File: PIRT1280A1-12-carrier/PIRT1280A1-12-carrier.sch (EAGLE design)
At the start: 124 parts, among them J1 5-1734592-0, U1 LT3042IMSE#TRPBF, U2 LT3042IMSE#TRPBF, U3 LT3042IMSE#TRPBF, U4 LT3042IMSE#TRPBF, U5 LT3042IMSE#TRPBF, U6 DS90CR218AMTD/NOPBMTD48_TEX-L

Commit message: mostly finished with PIRT1280 carrier
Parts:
- removed C38: 10u, oresat-rcl:C-EU0603-C-NOSILK
- removed SJ11, SJ12, SJ13, SJ14, SJ15, SJ22: SOLDERJUMPERNC, SparkFun-Passives:SOLDERJUMPERNC
- removed TEC+, TEC-, VDETCOM, VPH, VPL, VPOS, VPOUT: TEST-POINT_SMD-SMD-10SN, oresat-misc:TEST-POINT_SMD-SMD-10SN
- removed TP39, TP40, TP41, TP42, TP43: TEST-POINT-LARGE-SQUARE, oresat-misc:TEST-POINT-LARGE-SQUARE
- added C16: 1u, oresat-rcl:C-EU0603-A
- added C17: 0.1u, oresat-rcl:C-EU0603-A
- added C18: 1n, oresat-rcl:C-EU0402-C-NOSILK
- added D1: GREEN, SparkFun-LED:LED-GREEN0603
- added J10, J3, J4, J5, J6: 455-1750-1-ND, SparkFun-Connectors:CONN_03
- added J11: USB_A_SMT_FEMALE, SparkFun-Connectors:USB_A_SMT_FEMALE
- added J12: (no value), SparkFun-Connectors:CONN_025MM
- added J13: POWER_JACK, SparkFun-Connectors:POWER_JACK
- added J2: (no value), SparkFun-Connectors:CONN_02
- added J7: (no value), SparkFun-Connectors:CONN_05
- added J8: (no value), SparkFun-Connectors:CONN_13
- added J9: 5-1734592-0, J-TEConnectivity-X-1734592-X:5-1734592-0
- added JP1, JP100, JP101: JUMPER-SMT_2_NC_TRACE_NO-SILK, SparkFun-Jumpers:JUMPER-SMT_2_NC_TRACE_NO-SILK
- added Q1: 35A/25V/8.5mΩ, Q-Fairchild-FDD8780-MOSFET-NCH:MOSFET-NCH-FDD8780
- added R100, R101, R21, R22, R23, R24, R25, R26: 100, oresat-rcl:R-US_0402-C-NOSILK
- added R12: NP, oresat-rcl:R-US_0603-A
- added R19: 10k, R-Panasonic-EXB_A10PXXXJ:EXB-A10P391JC_ARRAY_EXBA-M
- added R20: TBD, oresat-rcl:R-US_0603-A
- added REFCLK, THERM+, THERM-, TP9: TEST-POINT-LARGE-SQUARE, oresat-misc:TEST-POINT-LARGE-SQUARE
- added TP100, TP101, TP102, TP103, TP104, TP105, TP106, TP107: TEST-POINT-SMD-0.5MM, oresat-misc:TEST-POINT-SMD-0.5MM
- added U7: DS90CR218AMTD/NOPBMTD48_TEX-L, U-TI-DS90CR218-LVDSReceiver:DS90CR218AMTD/NOPBMTD48_TEX-L
- added X1: 16MHz, X-OSCILLATOR-GENERIC:OSC_GENERIC_2.5X2.0
- C1, C10, C2, C3, C4, C5, C6, C7, C8, C9: device oresat-rcl:C-EU0402-A-NOSILK -> oresat-rcl:C-EU0603-A
- C11, C12, C13, C14, C15: value 4.7u -> 0.47u; device oresat-rcl:C-EU0402-A-NOSILK -> oresat-rcl:C-EU0603-A
- C19, C22: value 1n -> 10n; DPN 490-6350-1-ND -> 399-7842-1-ND; MFR Murata -> Kemet; MPN GRM155R71H102KA01J -> C0603C103M5RACTU
- C20, C23: value 1n -> 100n; DPN 490-6350-1-ND -> 399-1177-1-ND; MFR Murata -> Kemet; MPN GRM155R71H102KA01J -> C0805C104Z5VACTU
- C24: value 1n -> 10u; device oresat-rcl:C-EU0402-C-NOSILK -> oresat-rcl:C-EU0603-C-NOSILK; DPN 490-6350-1-ND -> 490-14372-1-ND; MPN GRM155R71H102KA01J -> GRM188R61A106KE69J
- C25, C30: value 10n -> 100n; DPN 399-7842-1-ND -> 399-1177-1-ND; MPN C0603C103M5RACTU -> C0805C104Z5VACTU
- C27, C28: value 10n -> 1n; DPN 399-7842-1-ND -> 490-6350-1-ND; MFR Kemet -> Murata; MPN C0603C103M5RACTU -> GRM155R71H102KA01J
- C31, C36: value 100n -> 1n; DPN 399-1177-1-ND -> 490-6350-1-ND; MFR Kemet -> Murata; MPN C0805C104Z5VACTU -> GRM155R71H102KA01J
- C32, C35: value 100n -> 10n; DPN 399-1177-1-ND -> 399-7842-1-ND; MPN C0805C104Z5VACTU -> C0603C103M5RACTU
- J1: value 5-1734592-0 -> 455-1750-1-ND; device J-TEConnectivity-X-1734592-X:5-1734592-0 -> SparkFun-Connectors:CONN_03
- R1: value (none) -> 1k; device oresat-rcl:R-US_0603-A-NOSILK -> oresat-rcl:R-US_0603-A
- R10, R11, R8, R9: value 100 -> NP; device oresat-rcl:R-US_0402-C-NOSILK -> oresat-rcl:R-US_0603-A; DIS Dgi-Key -> (none); DPN 311-100MCT-ND -> (none); MFR Yageo -> (none); MPN RC0201FR-07100RL -> (none)
- R13, R14: value 100 -> 0; device oresat-rcl:R-US_0402-C-NOSILK -> oresat-rcl:R-US_0603-A; DIS Dgi-Key -> (none); DPN 311-100MCT-ND -> (none); MFR Yageo -> (none); MPN RC0201FR-07100RL -> (none)
- R15, R17: device oresat-rcl:R-US_0603-A-NOSILK -> oresat-rcl:R-US_0603-A
- R16: value (none) -> 0; device oresat-rcl:R-US_0603-A-NOSILK -> oresat-rcl:R-US_0603-A
- R18: value 100 -> 20k; device oresat-rcl:R-US_0402-C-NOSILK -> oresat-rcl:R-US_0805-A; DIS Dgi-Key -> (none); DPN 311-100MCT-ND -> (none); MFR Yageo -> (none); MPN RC0201FR-07100RL -> (none)
- R2: value 0 -> 10k; device oresat-rcl:R-US_0603-A-NOSILK -> R-Panasonic-EXB-2HV103JV:EXB-2HV103JV
- R3: value (none) -> 29.4k; device oresat-rcl:R-US_0603-A-NOSILK -> oresat-rcl:R-US_0603-A
- R4: value (none) -> 9.09k; device oresat-rcl:R-US_0603-A-NOSILK -> oresat-rcl:R-US_0603-A
- R5: value 0 -> 16.2k; device oresat-rcl:R-US_0603-A-NOSILK -> oresat-rcl:R-US_0603-A
- R6: value (none) -> 33.2k; device oresat-rcl:R-US_0603-A-NOSILK -> oresat-rcl:R-US_0603-A
- R7: value 0 -> 33.2k; device oresat-rcl:R-US_0603-A-NOSILK -> oresat-rcl:R-US_0603-A
- SJ1, SJ10, SJ2, SJ3, SJ4, SJ5, SJ6, SJ7, SJ8, SJ9: value SOLDERJUMPERNC -> JUMPER-SMT_2_NC_TRACE_NO-SILK; device SparkFun-Passives:SOLDERJUMPERNC -> SparkFun-Jumpers:JUMPER-SMT_2_NC_TRACE_NO-SILK
- U6: value DS90CR218AMTD/NOPBMTD48_TEX-L -> LM2901QPWRQ1PW14-M; device U-TI-DS90CR218-LVDSReceiver:DS90CR218AMTD/NOPBMTD48_TEX-L -> U-TI-LM2901:LM2901QPWRQ1PW14-M
- renumbered U$1 to U$2
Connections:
- removed net CLK: U$2G$1.P1_20, U6.RXCLKOUT
- removed net D0: U$2G$1.P1_36, U6.RXOUT0
- removed net D1: U$2G$1.P1_33, U6.RXOUT1
- removed net D2: U$2G$2.P2_32, U6.RXOUT2
- removed net D3: U$2G$2.P2_30, U6.RXOUT3
- removed net D4: U$2G$1.P1_31, U6.RXOUT4
- removed net D5: U$2G$2.P2_34, U6.RXOUT5
- removed net D6: U$2G$2.P2_28, U6.RXOUT6
- removed net D7: U$2G$1.P1_29, U6.RXOUT7
- removed net N$30: SJ11.1, TP32.1, U4.EN/UV
- removed net N$34: U6.!PWR_DWN
- removed net SDCLK: J1.49, TP4.1
- removed net SDIN: J1.50, TP5.1
- removed net SDOUT: J1.48, TP6.1
- removed net USB_D+: U$2G$1.P1_11
- removed net USB_D-: U$2G$1.P1_9
- new net !PWR_DWN: J3.2, R19.11, U7.!PWR_DWN
- new net 1.8V-A: R20.2, U$2G$1.P1_18
- new net N$1: R2.1, R2.2
- new net N$2: R2.15, R2.3, U6.4IN-
- new net N$270: D1.A, R1.1
- new net N$3: R2.14, R2.4, U6.3IN-
- new net N$4: R2.13, R2.5, U6.2IN-
- new net N$41: J13.PWR, U$2G$1.P1_1
- new net N$44: R2.11, R2.12, U6.1IN-
- new net N$47: TP100.TP, U7.RXOUT7
- new net N$48: TP101.TP, U7.RXOUT8
- new net N$49: TP102.TP, U7.RXOUT9
- new net N$5: C16.1, R18.2, U6.1IN+, U6.2IN+, U6.3IN+, U6.4IN+
- new net N$50: TP103.TP, U7.RXOUT10
- new net N$51: TP104.TP, U7.RXOUT11
- new net N$52: TP105.TP, U7.RXOUT12
- new net N$53: TP106.TP, U7.RXOUT13
- new net N$54: TP107.TP, U7.RXOUT14
- new net N$55: J2.2, U$2G$1.P1_34
- new net N$56: J10.1, Q1.D
- new net N$58: J3.1, U$2G$2.P2_20
- new net N$6: R2.6, R2.7
- new net N$8: JP100.1, U$2G$1.P1_5
- new net PRU0: J8.2, U$2G$1.P1_36, U7.RXOUT0
- new net PRU1: J8.3, U$2G$1.P1_33, U7.RXOUT1
- new net PRU14_OUT: J8.11, U$2G$2.P2_24
- new net PRU15_OUT: J8.12, U$2G$2.P2_33
- new net PRU16_CLK: J8.9, U$2G$1.P1_20, U7.RXCLKOUT
- new net PRU2: J8.4, U$2G$2.P2_32, U7.RXOUT2
- new net PRU3: J8.5, U$2G$2.P2_30, U7.RXOUT3
- new net PRU4: J8.6, U$2G$1.P1_31, U7.RXOUT4
- new net PRU5: J8.7, U$2G$2.P2_34, U7.RXOUT5
- new net PRU6: J8.8, U$2G$2.P2_28, U7.RXOUT6
- new net PRU7: J8.10, U$2G$1.P1_29
- new net PRU_UART_RX: J6.2, U$2G$1.P1_12
- new net PRU_UART_TX: J6.1, U$2G$1.P1_6
- new net REFCLK_ENABLE: R19.33, TP27.1, TP28.1, U6.OUT4, X1.EN
- new net SENSOR_ENABLE: J4.1, U$2G$1.P1_28
- new net TEC_ENABLE: Q1.G, R19.22, U$2G$1.P1_35
- new net TEC_GND: J10.3, J12.1, Q1.S
- new net UART0_RX: J5.2, U$2G$1.P1_32
- new net UART0_TX: J5.1, U$2G$1.P1_30
- new net USB_N: J11.D-, U$2G$1.P1_9
- new net USB_P: J11.D+, U$2G$1.P1_11
- net 3.3V: now also C18.1, J3.3, J4.3, R2.16, U7.LVDS_VCC, U7.PLL_VCC, U7.VCC, U7.VCC_2, U7.VCC_3, U7.VCC_4, X1.VCC; no longer C38.1, U6.LVDS_VCC, U6.PLL_VCC, U6.VCC_2, U6.VCC_3, U6.VCC_4
- net 5V: now also C2.1, C3.1, C5.1, J11.VBUS, JP100.2, SJ10.2, SJ7.2, TP15.1, TP3.1, TP6.1, TP9.1, U$2G$1.P1_24, U$2G$2.P2_13; no longer C10.1, C13.1, C7.1, SJ11.2, SJ12.2, SJ14.2, SJ15.2, SJ2.2, SJ3.2, SJ5.2, TP19.1, TP26.1, TP33.1, TP40.1, U$2G$1.P1_7
- net CAN_RX: now also J1.2
- net CAN_TX: now also J1.1
- net GND: now also C16.2, C17.2, C18.2, D1.C, J11.GND, J11.SHIELD, J13.GND, J13.GNDBREAK, J5.3, J6.3, J7.5, J8.1, J8.13, J9.1, J9.10, J9.13, J9.16, J9.19, J9.2, J9.22, J9.25, J9.28, J9.3, J9.31, J9.34, J9.37, J9.40, J9.44, J9.48, J9.7, J9.PAD, JP1.1, JP101.2, R10.1, R11.1, R12.1, R19.55, R2.10, R5.1, R7.1, R8.1, R9.1, SJ2.1, SJ3.1, SJ5.1, U$2G$1.P1_16, U7.GND, X1.GND; no longer C38.2, J1.12, J1.15, J1.19, J1.23, J1.27, J1.31, J1.35, J1.39, J1.43, J1.6, J1.9, J1.PAD, R1.1, R16.1, SJ10.1, SJ13.1, SJ7.1
- net JAMSYNC: now also J2.1, J9.49; no longer J1.47, TP7.1
- net N$10: now also R19.77, TP20.1, TP21.1, U1.EN/UV, U6.OUT3; no longer SJ5.1, TP18.1, U2.EN/UV
- net N$11: now also SJ7.1, TP31.1, U5.PGFB; no longer SJ3.1, TP15.1, U1.PGFB
- net N$12: now also SJ2.2, TP4.1, U5.ILIM; no longer SJ1.2, TP14.1, U1.ILIM
- net N$13: now also R100.2, U7.RXIN2-; no longer R9.2, U6.RXIN2-
- net N$14: now also R100.1, U7.RXIN2+; no longer R9.1, U6.RXIN2+
- net N$15: now also TP5.1, U5.PG; no longer TP10.1, U1.PG
- net N$16: now also JP101.1, U$2G$1.P1_13; no longer U$2G$1.P1_16
- net N$17: now also J4.2, R18.1; no longer U$2G$1.P1_3, U$2G$1.P1_5
- net N$18: now also R101.2, U7.RXIN1-; no longer R10.2, U6.RXIN1-
- net N$19: now also R101.1, U7.RXIN1+; no longer R10.1, U6.RXIN1+
- net N$20: now also C12.1, R4.2, R9.2, TP32.1, U5.SET; no longer C2.1, R3.2, TP1.1, U1.SET
- net N$21: now also SJ1.2, TP1.1, U1.ILIM; no longer SJ4.2, TP21.1, U2.ILIM
- net N$22: now also TP29.1, U1.PGFB; no longer TP22.1, U2.PGFB
- net N$23: now also TP2.1, U1.PG; no longer TP17.1, U2.PG
- net N$24: now also C11.1, R3.2, R8.2, TP30.1, U1.SET; no longer C5.1, R1.2, TP16.1, U2.SET
- net N$25: now also R1.2, R19.66, TP16.1, TP17.1, U3.EN/UV, U4.EN/UV, U6.OUT1; no longer SJ8.1, TP25.1, U5.EN/UV
- net N$26: now also SJ5.2, TP13.1, U4.ILIM; no longer SJ7.2, TP28.1, U5.ILIM
- net N$27: now also SJ10.1, TP37.1, U4.PGFB; no longer SJ9.1, TP29.1, U5.PGFB
- net N$28: now also TP14.1, U4.PG; no longer TP24.1, U5.PG
- net N$29: now also C15.1, R12.2, R7.2, TP38.1, U4.SET; no longer C8.1, R4.2, TP23.1, U5.SET
- net N$31: now also SJ4.2, TP10.1, U3.ILIM; no longer SJ10.2, TP35.1, U4.ILIM
- net N$32: now also SJ9.1, TP35.1, U3.PGFB; no longer SJ12.1, TP36.1, U4.PGFB
- net N$33: now also TP11.1, U3.PG; no longer TP31.1, U4.PG
- net N$35: now also C14.1, R11.2, TP36.1, U3.SET; no longer C11.1, TP30.1, U4.SET
- net N$36: now also R19.44, TP18.1, TP19.1, U2.EN/UV, U5.EN/UV, U6.OUT2; no longer SJ14.1, TP39.1, U3.EN/UV
- net N$37: now also SJ3.2, TP7.1, U2.ILIM; no longer SJ13.2, TP42.1, U3.ILIM
- net N$38: now also SJ8.1, TP33.1, U2.PGFB; no longer SJ15.1, TP43.1, U3.PGFB
- net N$39: now also TP8.1, U2.PG; no longer TP38.1, U3.PG
- net N$40: now also C13.1, R10.2, R5.2, TP34.1, U2.SET; no longer C14.1, R16.2, TP37.1, U3.SET
- net N$9: now also R26.1, X1.OUT; no longer SJ2.1, TP11.1, U1.EN/UV
- net OUT1_N: now also J9.27, R24.2, U7.RXIN0-; no longer J1.11, R8.2, U6.RXIN0-
- net OUT1_P: now also J9.26, R24.1, U7.RXIN0+; no longer J1.10, R8.1, U6.RXIN0+
- net OUT2_N: now also J9.24, R23.1; no longer J1.8, R13.2
- net OUT2_P: now also J9.23, R23.2; no longer J1.7, R13.1
- net OUT3_N: now also J9.21, R22.1; no longer J1.5, R14.2
- net OUT3_P: now also J9.20, R22.2; no longer J1.4, R14.1
- net OUT4_N: now also J9.18, R21.1; no longer J1.2, R18.2
- net OUT4_P: now also J9.17, R21.2; no longer J1.1, R18.1
- net REFCLK: now also J9.50, R26.2, REFCLK.1; no longer J1.46, TP8.1
- net SPI1_CLK: now also J7.2, J9.5
- net SPI1_CS1: now also J7.4
- net SPI1_MISO: now also J7.3, J9.6
- net SPI1_MOSI: now also J7.1, J9.4
- net TEC+: now also J12.2, J9.45, J9.46, J9.47; no longer J1.40, J1.41, J1.42, TEC+.TP
- net TEC-: now also J10.2, J9.41, J9.42, J9.43; no longer J1.36, J1.37, J1.38, TEC-.TP
- net THERM+: now also C17.1, J9.9, R20.1, THERM+.1, U$2G$1.P1_17; no longer J1.45, TP2.1
- net THERM-: now also J9.8, JP1.2, THERM-.1; no longer J1.44, TP3.1
- net TXCLK_N: now also J9.30, R25.1, U7.RXCLKIN-; no longer J1.14, R11.1, U6.RXCLKIN-
- net TXCLK_P: now also J9.29, R25.2, U7.RXCLKIN+; no longer J1.13, R11.2, U6.RXCLKIN+
- net VDETCOM: now also R13.2, TP22.1, U1.OUT, U1.OUTS; no longer J1.28, J1.29, J1.30, R2.2, TP20.1, U2.OUT, U2.OUTS, VDETCOM.TP
- net VDETCOM-2.9V: now also J9.11, J9.12, R13.1; no longer R2.1
- net VPH: now also C9.1, R16.2, TP25.1, U3.OUT, U3.OUTS; no longer C12.1, J1.24, J1.25, J1.26, R15.2, TP34.1, U4.OUT, U4.OUTS, VPH.TP
- net VPH-3.3V: now also J9.35, J9.36, R16.1; no longer R15.1
- net VPL: now also C8.1, R15.2, TP24.1, U2.OUT, U2.OUTS; no longer C15.1, J1.20, J1.21, J1.22, R17.2, TP41.1, U3.OUT, U3.OUTS, VPL.TP
- net VPL-1.6V: now also J9.32, J9.33, R15.1; no longer R17.1
- net VPOS: now also C10.1, R17.2, TP26.1, U4.OUT, U4.OUTS; no longer C9.1, J1.32, J1.33, J1.34, R5.2, TP27.1, U5.OUT, U5.OUTS, VPOS.TP
- net VPOS-3.3V: now also J9.38, J9.39, R17.1; no longer R5.1
- net VPOUT: now also C7.1, R14.2, TP23.1, U5.OUT, U5.OUTS; no longer C3.1, J1.16, J1.17, J1.18, R7.2, TP13.1, U1.OUT, U1.OUTS, VPOUT.TP
- net VPOUT-0.9V: now also J9.14, J9.15, R14.1; no longer R7.1
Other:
- note added: "!PWR_DWN is pulled low by default, but can be pulled high via jumper or via GPIO NOTE: Pull down on other sheet"
- note added: "16MHz Oscillator"
- note added: "5V barrel jack"
- note added: "<-- To PIRT1280 Thermistor"
- note added: "CAN0"
- note added: "Initially unconnected until we test SPI"
- note added: "JAMSYNC jumper for manual or GPIO operation"
- note added: "Jumper to enable sensor power manually or via GPIO"
- note added: "Only need to connect 7 bits"
- note added: "POWER UP/DOWN SEQUENCE: - VPOS, VPH - VPL, VPOUT - VDETCOM - REFCLK"
- note added: "PRU UART"
- note added: "RC circuit that raises voltage to all IN+ inputs at a set rate"
- note added: "TEC"
- note added: "TEC Screw Terminal 8.2VDC at 27C, 9.2VDC at 50C"
- note added: "TEC can be enabled with a jumper or via MOSFET + GPIO"
- note added: "TODO need thermistor specs"
- note added: "TODO what about CS?"
- note added: "To other sheet"
- note added: "UART0"
- note added: "USB Host"
- note removed: "TODO double check USB V_EN to USB VBUS"
- note removed: "TODO what to do with unconnected?"
- note removed: "TODO when asserted, PWR_DWN will drive outputs low, so maybe pull high but add a jumper to drive low?"

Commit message: touch ups
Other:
- note added: "50 pin breakout connector"
- note added: "DESERIALIZER"
- note added: "POCKETBEAGLE"
- note added: "POWER SEQUENCER"
- note added: "PWR + USB"
- note removed: "Pocket Beagle Connector"
- note removed: "Pocketbeagle has internal 3.3V LDO that will supply the board (500mA MAX)"
- note removed: "TODO renumber"

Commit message: address review comments
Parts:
- added C37: 1n, oresat-rcl:C-EU0402-C-NOSILK
- added C38, C39: NP, oresat-rcl:C-EUC1210
- added C40: 0.1u, oresat-rcl:C-EU0603-A
- added D2: GREEN, SparkFun-LED:LED-GREEN0603
- added FB1: (no value), oresat-rcl:L-BEAD-0805-B
- added J14: POWER_JACK, SparkFun-Connectors:POWER_JACK
- added R27: 100, oresat-rcl:R-US_0402-C-NOSILK
- added R28: 1k, oresat-rcl:R-US_0603-A
- C11: value 0.47u -> 0.1u
- C16: value 1u -> 0.47u
- C17: value 0.1u -> 1u
- C18: value 1n -> 0.1u; device oresat-rcl:C-EU0402-C-NOSILK -> oresat-rcl:C-EU0603-A; DIS Digi-Key -> (none); DPN 490-6350-1-ND -> (none); MFR Murata -> (none); MPN GRM155R71H102KA01J -> (none)
- C19, C22, C29, C32: value 10n -> 1n; DPN 399-7842-1-ND -> 490-6350-1-ND; MFR Kemet -> Murata; MPN C0603C103M5RACTU -> GRM155R71H102KA01J
- C20, C23, C30, C33: value 100n -> 10n; DPN 399-1177-1-ND -> 399-7842-1-ND; MPN C0805C104Z5VACTU -> C0603C103M5RACTU
- C21, C31: value 1n -> 100n; DPN 490-6350-1-ND -> 399-1177-1-ND; MFR Murata -> Kemet; MPN GRM155R71H102KA01J -> C0805C104Z5VACTU
- C24: value 10u -> 100n; device oresat-rcl:C-EU0603-C-NOSILK -> oresat-rcl:C-EU0402-C-NOSILK; DPN 490-14372-1-ND -> 399-1177-1-ND; MFR Murata -> Kemet; MPN GRM188R61A106KE69J -> C0805C104Z5VACTU
- C25: value 100n -> 10u; device oresat-rcl:C-EU0402-C-NOSILK -> oresat-rcl:C-EU0603-C-NOSILK; DPN 399-1177-1-ND -> 490-14372-1-ND; MFR Kemet -> Murata; MPN C0805C104Z5VACTU -> GRM188R61A106KE69J
- C26, C35: value 10n -> 100n; DPN 399-7842-1-ND -> 399-1177-1-ND; MPN C0603C103M5RACTU -> C0805C104Z5VACTU
- C27, C36: value 1n -> 10n; DPN 490-6350-1-ND -> 399-7842-1-ND; MFR Murata -> Kemet; MPN GRM155R71H102KA01J -> C0603C103M5RACTU
- J11: value USB_A_SMT_FEMALE -> (none); device SparkFun-Connectors:USB_A_SMT_FEMALE -> SparkFun-Connectors:CONN_02; DESCRIPTION SparkFun Accessories USB Female Type A SMD Connector -> (none); MANUFACTURER SparkFun -> (none); MANUFACTURER_PART_NUMBER PRT-09011 -> (none); MOUSER_PART_NUMBER 474-PRT-09011 -> (none)
- J12: value (none) -> USB_A_SMT_FEMALE; device SparkFun-Connectors:CONN_025MM -> SparkFun-Connectors:USB_A_SMT_FEMALE; DESCRIPTION (none) -> SparkFun Accessories USB Female Type A SMD Connector; MANUFACTURER (none) -> SparkFun; MANUFACTURER_PART_NUMBER (none) -> PRT-09011; MOUSER_PART_NUMBER (none) -> 474-PRT-09011
- J13: value POWER_JACK -> (none); device SparkFun-Connectors:POWER_JACK -> SparkFun-Connectors:CONN_025MM
- J5: value 455-1750-1-ND -> (none); device SparkFun-Connectors:CONN_03 -> SparkFun-Connectors:CONN_04PTH
- R18: value 20k -> 200k
- R19: value 10k -> 20k; device R-Panasonic-EXB_A10PXXXJ:EXB-A10P391JC_ARRAY_EXBA-M -> oresat-rcl:R-US_0805-A
- R20: value TBD -> 10k; device oresat-rcl:R-US_0603-A -> R-Panasonic-EXB_A10PXXXJ:EXB-A10P391JC_ARRAY_EXBA-M
- R21: value 100 -> TBD; device oresat-rcl:R-US_0402-C-NOSILK -> oresat-rcl:R-US_0603-A; DIS Dgi-Key -> (none); DPN 311-100MCT-ND -> (none); MFR Yageo -> (none); MPN RC0201FR-07100RL -> (none)
- R22, R23, R24, R29, R30: value 100 -> NP
- renumbered JP100 to JP2, JP101 to JP3, R100 to R29, R101 to R30, TP100 to TP39, TP101 to TP40, TP102 to TP41, TP103 to TP42, TP104 to TP43, TP105 to TP44, TP106 to TP45, TP107 to TP46
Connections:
- net N$58 renamed SERDES_PWR_DOWN
- removed net N$41: J13.PWR, U$2G$1.P1_1
- new net N$30: J11.1, U$2G$1.P1_1
- new net N$34: D2.A, R28.1
- new net N$7: FB1.1, J11.2, J14.PWR, R28.2
- new net VDD: J12.VBUS, JP2.2, U$2G$1.P1_24, U$2G$2.P2_13
- net !PWR_DWN: now also R20.11; no longer R19.11
- net 1.8V-A: now also R21.2; no longer R20.2
- net 3.3V: now also C11.1, C37.1, C40.1, J5.1; no longer C18.1
- net 5V: now also C38.1, C39.1, FB1.2; no longer J11.VBUS, JP2.2, U$2G$1.P1_24, U$2G$2.P2_13
- net GND: now also C37.2, C38.2, C39.2, C40.2, D2.C, J12.GND, J12.SHIELD, J14.GND, J14.GNDBREAK, J5.4, R18.1, R20.55; no longer J11.GND, J11.SHIELD, J13.GND, J13.GNDBREAK, J5.3, R19.55
- net N$10: now also R20.77; no longer R19.77
- net N$11: now also U2.PGFB; no longer U5.PGFB
- net N$12: now also U2.ILIM; no longer U5.ILIM
- net N$15: now also U2.PG; no longer U5.PG
- net N$17: now also R19.1; no longer R18.1
- net N$20: now also C13.1, U2.SET; no longer C12.1, U5.SET
- net N$24: now also C12.1; no longer C11.1
- net N$25: now also R20.66, U5.EN/UV; no longer R19.66, U3.EN/UV
- net N$26: now also U5.ILIM; no longer U4.ILIM
- net N$27: now also U5.PGFB; no longer U4.PGFB
- net N$28: now also U5.PG; no longer U4.PG
- net N$29: now also C16.1, U5.SET; no longer C15.1, U4.SET
- net N$31: now also U4.ILIM; no longer U3.ILIM
- net N$32: now also U4.PGFB; no longer U3.PGFB
- net N$33: now also U4.PG; no longer U3.PG
- net N$35: now also C15.1, U4.SET; no longer C14.1, U3.SET
- net N$36: now also R20.44, U3.EN/UV; no longer R19.44, U5.EN/UV
- net N$37: now also U3.ILIM; no longer U2.ILIM
- net N$38: now also U3.PGFB; no longer U2.PGFB
- net N$39: now also U3.PG; no longer U2.PG
- net N$40: now also C14.1, U3.SET; no longer C13.1, U2.SET
- net N$5: now also C17.1, R19.2; no longer C16.1
- net N$9: now also R27.1; no longer R26.1
- net OUT1_N: now also R25.2; no longer R24.2
- net OUT1_P: now also R25.1; no longer R24.1
- net OUT2_N: now also R24.1; no longer R23.1
- net OUT2_P: now also R24.2; no longer R23.2
- net OUT3_N: now also R23.1; no longer R22.1
- net OUT3_P: now also R23.2; no longer R22.2
- net OUT4_N: now also R22.1; no longer R21.1
- net OUT4_P: now also R22.2; no longer R21.2
- net REFCLK: now also R27.2; no longer R26.2
- net REFCLK_ENABLE: now also R20.33; no longer R19.33
- net TEC+: now also J13.2; no longer J12.2
- net TEC_ENABLE: now also R20.22; no longer R19.22
- net TEC_GND: now also J13.1; no longer J12.1
- net THERM+: now also C18.1, R21.1; no longer C17.1, R20.1
- net TXCLK_N: now also R26.1; no longer R25.1
- net TXCLK_P: now also R26.2; no longer R25.2
- net UART0_RX: now also J5.3; no longer J5.2
- net UART0_TX: now also J5.2; no longer J5.1
- net USB_N: now also J12.D-; no longer J11.D-
- net USB_P: now also J12.D+; no longer J11.D+
- net VPH: now also U4.OUT, U4.OUTS; no longer U3.OUT, U3.OUTS
- net VPL: now also U3.OUT, U3.OUTS; no longer U2.OUT, U2.OUTS
- net VPOS: now also U5.OUT, U5.OUTS; no longer U4.OUT, U4.OUTS
- net VPOUT: now also U2.OUT, U2.OUTS; no longer U5.OUT, U5.OUTS
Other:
- note added: "POCKETBEAGLE POWER JUMPER"
- note added: "TEC Screw Terminal 8.2VDC at 27C, 9.2VDC at 50C 2.5A"
- note removed: "TEC Screw Terminal 8.2VDC at 27C, 9.2VDC at 50C"
- moved on the sheet: C12, C13, C14, C15, C16, C18, C19, C20, C21, C22, C23, C24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

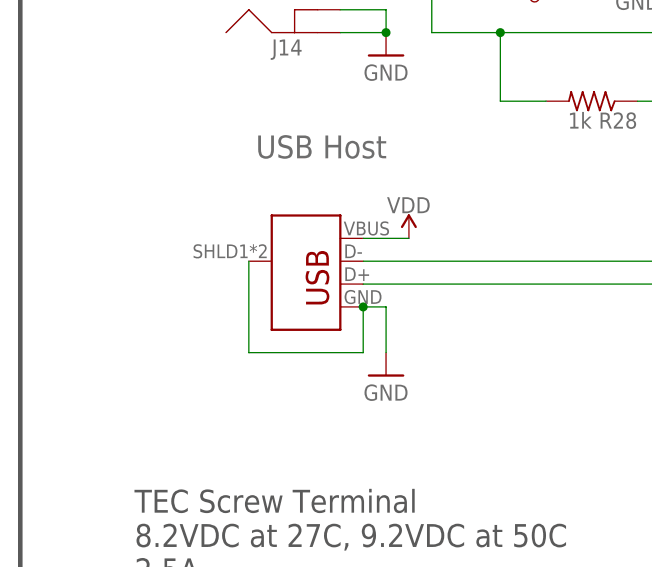
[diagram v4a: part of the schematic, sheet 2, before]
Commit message: added PIRT1280 BOM, used internal library in carrier, added attributes
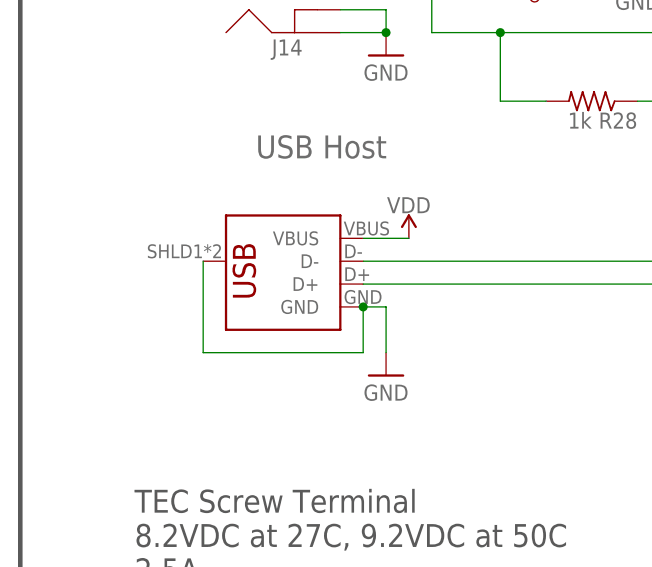
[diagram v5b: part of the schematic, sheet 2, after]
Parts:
- J12: device SparkFun-Connectors:USB_A_SMT_FEMALE -> J-Generic-USB_A_Female:USB_A_SMT_FEMALE; DPN (none) -> A115151-ND
- J13: device SparkFun-Connectors:CONN_025MM -> J-Generic-5mm-Screw-Terminal:5MM_SCREW_TERMINAL5MM; DPN (none) -> WM12755-ND; MPN (none) -> 0395430002
- J14: device SparkFun-Connectors:POWER_JACK -> J-Generic-5.5mm-Barrel-Jack:POWER_JACK
- R20: DPN (none) -> U7103CT-ND; MPN (none) -> EXB-A10P103J
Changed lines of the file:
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@@
 <?xml version="1.0" encoding="utf-8"?>
 <!DOCTYPE eagle SYSTEM "eagle.dtd">
-<eagle version="9.6.2">
+<eagle version="9.5.2">
 <drawing>
 <settings>
@@
 <part name="3.3V2" library="oresat-supplies" deviceset="3.3V" device=""/>
 <part name="GND42" library="supply" deviceset="GND" device=""/>
-<part name="R20" library="R-Panasonic-EXB_A10PXXXJ" deviceset="EXB-A10P391J" device="C_ARRAY_EXBA-M" value="10k"/>
+<part name="R20" library="R-Panasonic-EXB_A10PXXXJ" deviceset="EXB-A10P391J" device="C_ARRAY_EXBA-M" value="10k">
+<attribute name="DPN" value="U7103CT-ND"/>
+<attribute name="MPN" value="EXB-A10P103J"/>
+</part>
 <part name="GND5" library="supply" deviceset="GND" device=""/>
 <part name="R19" library="oresat-rcl" deviceset="R-US_" device="0805-A" value="20k"/>
@@
 <part name="JP2" library="SparkFun-Jumpers" deviceset="JUMPER-SMT_2_NC_TRACE" device="_NO-SILK"/>
 <part name="GND44" library="SparkFun-PowerSymbols" deviceset="GND" device=""/>
-<part name="J14" library="SparkFun-Connectors" deviceset="POWER_JACK" device="" value="POWER_JACK"/>
+<part name="J14" library="J-Generic-5.5mm-Barrel-Jack" deviceset="POWER_JACK" device="" value="POWER_JACK"/>
 <part name="GND45" library="SparkFun-PowerSymbols" deviceset="GND" device=""/>
-<part name="J12" library="SparkFun-Connectors" library_urn="urn:adsk.eagle:library:513" deviceset="USB_A" device="_SMT_FEMALE" package3d_urn="urn:adsk.eagle:package:38297/1" value="USB_A_SMT_FEMALE">
+<part name="J12" library="J-Generic-USB_A_Female" deviceset="USB_A" device="_SMT_FEMALE" value="USB_A_SMT_FEMALE">
 <attribute name="DESCRIPTION" value="SparkFun Accessories USB Female Type A SMD Connector"/>
+<attribute name="DPN" value="A115151-ND"/>
 <attribute name="MANUFACTURER" value="SparkFun"/>
 <attribute name="MANUFACTURER_PART_NUMBER" value="PRT-09011"/>
@@
 <part name="GND51" library="SparkFun-PowerSymbols" deviceset="GND" device=""/>
 <part name="Q1" library="Q-Fairchild-FDD8780-MOSFET-NCH" deviceset="MOSFET-NCH" device="-FDD8780" value="35A/25V/8.5mΩ"/>
-<part name="J13" library="SparkFun-Connectors" deviceset="CONN_02" device="5MM"/>
+<part name="J13" library="J-Generic-5mm-Screw-Terminal" deviceset="5MM_SCREW_TERMINAL" device="5MM">
+<attribute name="DPN" value="WM12755-ND"/>
+<attribute name="MPN" value="0395430002"/>
+</part>
 <part name="J2" library="SparkFun-Connectors" deviceset="CONN_02" device=""/>
 <part name="J10" library="SparkFun-Connectors" deviceset="CONN_03" device="" value="455-1750-1-ND"/>
@@
 <attribute name="VALUE" x="63.6016" y="48.3108" size="1.778" layer="96" font="vector" ratio="10" rot="SR0"/>
 <attribute name="NAME" x="63.4492" y="50.8508" size="1.778" layer="95" font="vector" ratio="10" rot="SR0"/>
+<attribute name="MPN" x="60.96" y="50.8" size="1.778" layer="96" rot="R270" display="off"/>
+<attribute name="DPN" x="60.96" y="50.8" size="1.778" layer="96" rot="R270" display="off"/>
 </instance>
 <instance part="GND5" gate="G1" x="50.8" y="45.72" smashed="yes"/>
@@
 <attribute name="MANUFACTURER_PART_NUMBER" x="17.78" y="-7.62" size="1.778" layer="96" rot="MR0" display="off"/>
 <attribute name="DESCRIPTION" x="17.78" y="-7.62" size="1.778" layer="96" rot="MR0" display="off"/>
+<attribute name="DPN" x="17.78" y="-7.62" size="1.778" layer="96" rot="MR0" display="off"/>
 </instance>
 <instance part="GND46" gate="1" x="27.94" y="-17.78" smashed="yes">
@@
 <attribute name="VALUE" x="15.24" y="-53.086" size="1.778" layer="96" font="vector"/>
 <attribute name="NAME" x="15.24" y="-42.672" size="1.778" layer="95" font="vector"/>
+<attribute name="DPN" x="17.78" y="-48.26" size="1.778" layer="96" display="off"/>
+<attribute name="MPN" x="17.78" y="-48.26" size="1.778" layer="96" display="off"/>
 </instance>
 <instance part="J2" gate="G$1" x="241.3" y="-48.26" smashed="yes" rot="MR0">
@@
 <wire x1="27.94" y1="-10.16" x2="27.94" y2="-15.24" width="0.1524" layer="91"/>
 <pinref part="J12" gate="G$1" pin="SHIELD"/>
-<wire x1="12.7" y1="-5.08" x2="12.7" y2="-15.24" width="0.1524" layer="91"/>
-<wire x1="12.7" y1="-15.24" x2="25.4" y2="-15.24" width="0.1524" layer="91"/>
+<wire x1="7.62" y1="-5.08" x2="7.62" y2="-15.24" width="0.1524" layer="91"/>
+<wire x1="7.62" y1="-15.24" x2="25.4" y2="-15.24" width="0.1524" layer="91"/>
 <wire x1="25.4" y1="-15.24" x2="25.4" y2="-10.16" width="0.1524" layer="91"/>
 <junction x="25.4" y="-10.16"/>
@@
 will not be understood (or retained) with this version.
 </note>
-<note version="8.3" severity="warning">
-Since Version 8.3, EAGLE supports the association of 3D packages
-with devices in libraries, schematics, and board files. Those 3D
-packages will not be understood (or retained) with this version.
-</note>
 </compatibility>

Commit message: rebase: backup work
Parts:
- R21: value TBD -> 10k
- U6: value LM2901QPWRQ1PW14-M -> TLC3704IPWRPW14-M; device U-TI-LM2901:LM2901QPWRQ1PW14-M -> U-TI-TLC3704:TLC3704IPWRPW14-M
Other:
- note removed: "TODO need thermistor specs"
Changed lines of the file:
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@@
 <?xml version="1.0" encoding="utf-8"?>
 <!DOCTYPE eagle SYSTEM "eagle.dtd">
-<eagle version="9.5.2">
+<eagle version="9.6.2">
 <drawing>
 <settings>
@@
 <part name="J7" library="SparkFun-Connectors" deviceset="CONN_05" device=""/>
 <part name="FRAME3" library="frames" library_urn="urn:adsk.eagle:library:229" deviceset="FRAME_C_L" device=""/>
-<part name="U6" library="U-TI-LM2901" deviceset="LM2901QPWRQ1" device="PW14-M"/>
+<part name="U6" library="U-TI-TLC3704" deviceset="TLC3704IPWR" device="PW14-M"/>
 <part name="3.3V1" library="oresat-supplies" deviceset="3.3V" device=""/>
 <part name="GND4" library="supply" deviceset="GND" device=""/>
@@
 <part name="JP1" library="SparkFun-Jumpers" deviceset="JUMPER-SMT_2_NC_TRACE" device="_NO-SILK"/>
 <part name="GND47" library="supply" deviceset="GND" device=""/>
-<part name="R21" library="oresat-rcl" deviceset="R-US_" device="0603-A" value="TBD"/>
+<part name="R21" library="oresat-rcl" deviceset="R-US_" device="0603-A" value="10k"/>
 <part name="1.8V-A1" library="oresat-supplies" deviceset="1.8V-A" device=""/>
 <part name="1.8V-A2" library="oresat-supplies" deviceset="1.8V-A" device=""/>
@@
 <text x="405.638" y="-332.74" size="1.778" layer="97" rot="R90">To other sheet</text>
 <text x="261.62" y="-248.92" size="5.08" layer="97">16MHz Oscillator</text>
-<text x="84.582" y="-24.13" size="2.54" layer="95">TODO need thermistor specs</text>
 <wire x1="152.4" y1="-297.18" x2="220.98" y2="-297.18" width="0.508" layer="97"/>
 <wire x1="220.98" y1="-297.18" x2="220.98" y2="-350.52" width="0.508" layer="97"/>
@@
 <instance part="R21" gate="R" x="109.22" y="-27.94" smashed="yes" rot="R90">
 <attribute name="NAME" x="107.7214" y="-31.75" size="1.778" layer="95" rot="R90"/>
-<attribute name="VALUE" x="115.062" y="-29.21" size="1.778" layer="96" rot="R90"/>
+<attribute name="VALUE" x="112.776" y="-29.464" size="1.778" layer="96" rot="R90"/>
 </instance>
 <instance part="1.8V-A1" gate="G$1" x="243.84" y="-5.08" smashed="yes">
